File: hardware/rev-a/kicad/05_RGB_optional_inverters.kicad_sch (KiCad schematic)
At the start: 15 parts, among them U10 NJM4580DD, U9 NJM4580DD

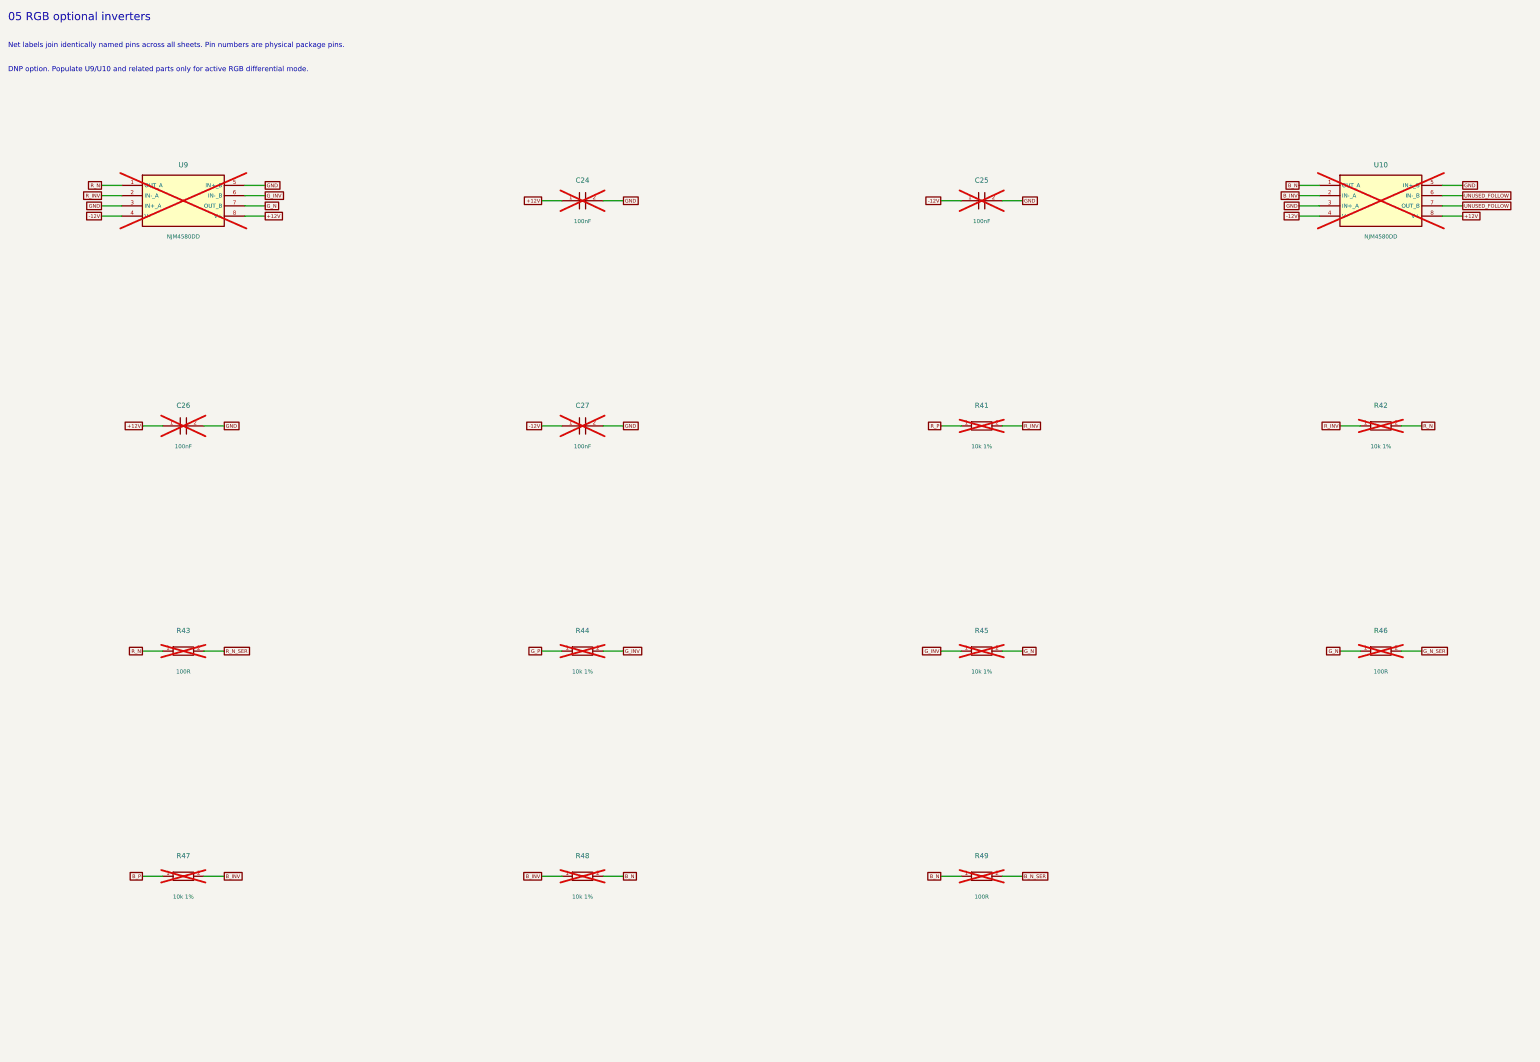
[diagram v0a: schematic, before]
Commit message: Redraw Rev.A schematics with functional blocks and explicit wiring
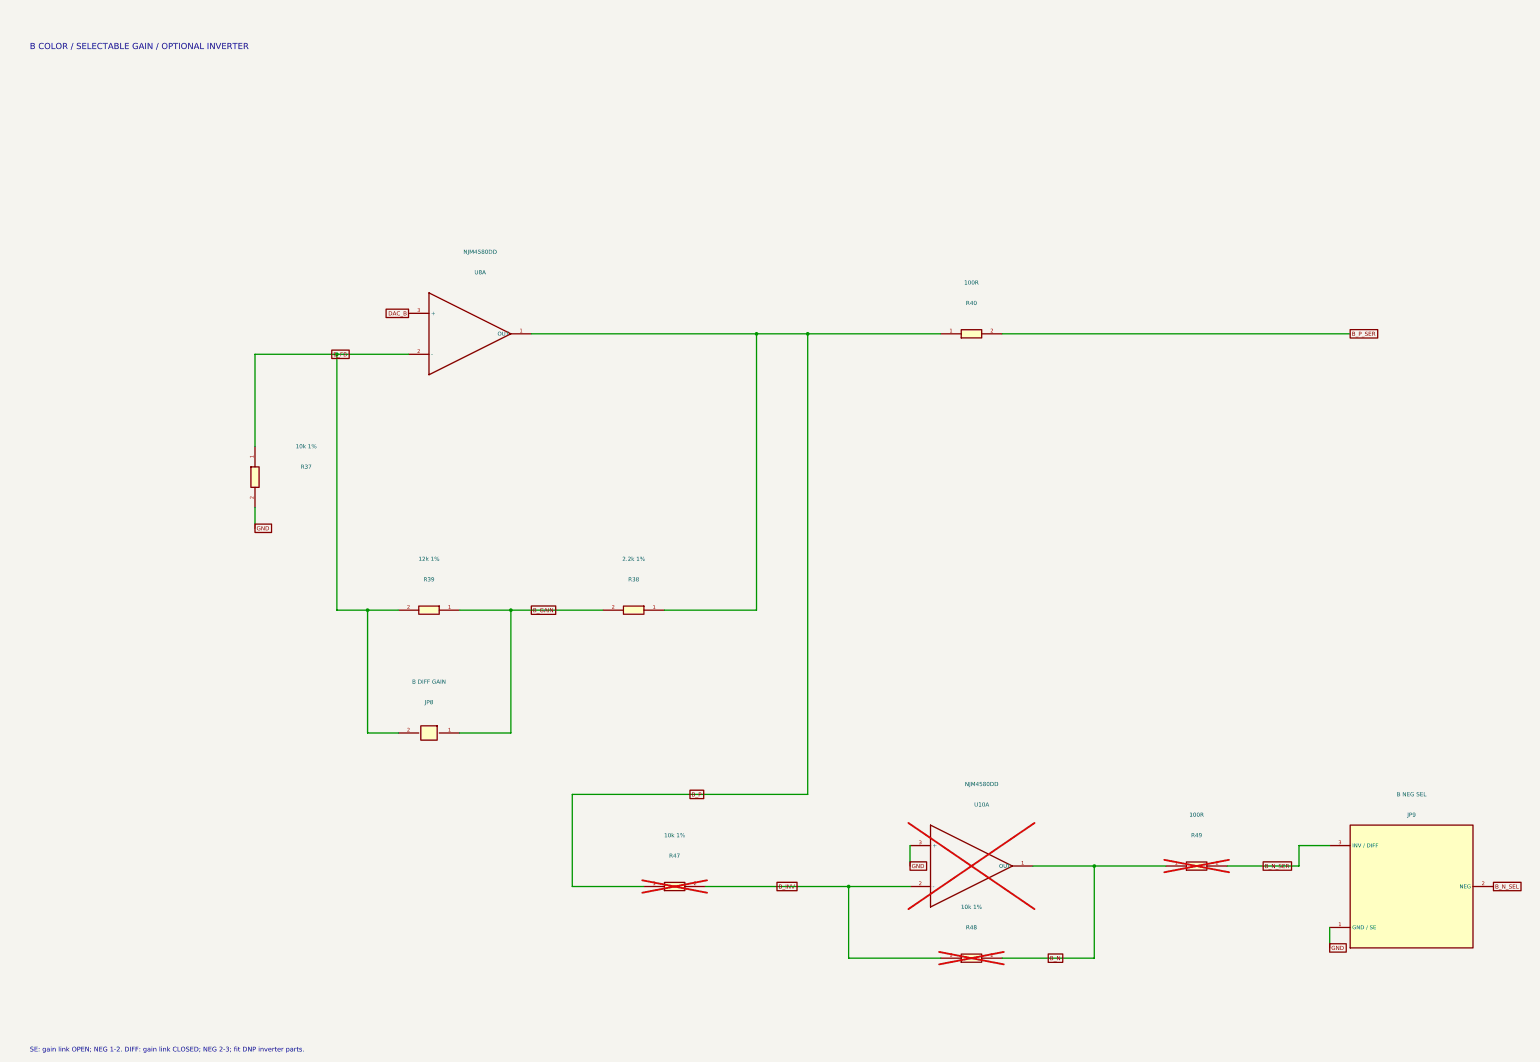
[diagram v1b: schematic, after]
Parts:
- removed C24, C25, C26, C27: 100nF, RevA:C_Disc_D5.0mm_W2.5mm_P5.00mm, symbol RevA:C
- removed R41, R42, R44, R45: 10k 1%, RevA:R_Axial_DIN0207_L6.3mm_D2.5mm_P10.16mm_Horizontal, symbol RevA:R
- removed R43, R46: 100R, RevA:R_Axial_DIN0207_L6.3mm_D2.5mm_P10.16mm_Horizontal, symbol RevA:R
- removed U9: NJM4580DD, RevA:DIP-8_W7.62mm, symbol RevA:Opamp
- added JP8: B DIFF GAIN, RevA:PinHeader_1x02_P2.54mm_Vertical, symbol RevA:Link
- added JP9: B NEG SEL, RevA:PinHeader_1x03_P2.54mm_Vertical, symbol RevA:Part_JP9
- added R37: 10k 1%, RevA:R_Axial_DIN0207_L6.3mm_D2.5mm_P10.16mm_Horizontal, symbol RevA:R
- added R38: 2.2k 1%, RevA:R_Axial_DIN0207_L6.3mm_D2.5mm_P10.16mm_Horizontal, symbol RevA:R
- added R39: 12k 1%, RevA:R_Axial_DIN0207_L6.3mm_D2.5mm_P10.16mm_Horizontal, symbol RevA:R
- added R40: 100R, RevA:R_Axial_DIN0207_L6.3mm_D2.5mm_P10.16mm_Horizontal, symbol RevA:R
- added U8: NJM4580DD, RevA:DIP-8_W7.62mm, symbol RevA:AMP
- U10: symbol RevA:Opamp -> RevA:AMP
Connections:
- net B_N_SER: now also JP9.3 (INV / DIFF)
- net B_P: now also R38.1, R40.1, U8.1 (OUT)
- net GND: now also JP9.1 (GND / SE), R37.2; no longer U10.5 (IN+_B)
- removed net +12V: U10.8 (V+)
- removed net -12V: U10.4 (V-)
- removed net UNUSED_FOLLOW: U10.6 (IN-_B), U10.7 (OUT_B)
- new net B_FB: JP8.2, R37.1, R39.2, U8.2 (-)
- new net B_GAIN: JP8.1, R38.2, R39.1
- new net B_N_SEL: JP9.2 (NEG)
- new net B_P_SER: R40.2
- new net DAC_B: U8.3 (+)
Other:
- note added: "B COLOR / SELECTABLE GAIN / OPTIONAL INVERTER"
- note added: "SE: gain link OPEN; NEG 1-2. DIFF: gain link CLOSED; NEG 2-3; fit DNP inverter parts."
- note removed: "05 RGB optional inverters"
- note removed: "DNP option. Populate U9/U10 and related parts only for active RGB differential mode."
- note removed: "Net labels join identically named pins across all sheets. Pin numbers are physical package pins."
- company: CoreS3 ILDA evaluation -> (none)
- title: 05_RGB_optional_inverters -> B / Color driver and optional differential stage
